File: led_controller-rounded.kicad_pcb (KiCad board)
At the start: 2 copper layers, 88.9 x 46.2 mm, 83 parts, among them J1 Screw_Terminal_01x02, J10 Conn_01x03, J2 SJ-3524-SMT, J3 Conn_01x03, J4 Conn_01x03, J5 Conn_01x03, J6 Conn_01x03, J7 Conn_01x03, J8 Conn_01x03, J9 Conn_01x03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

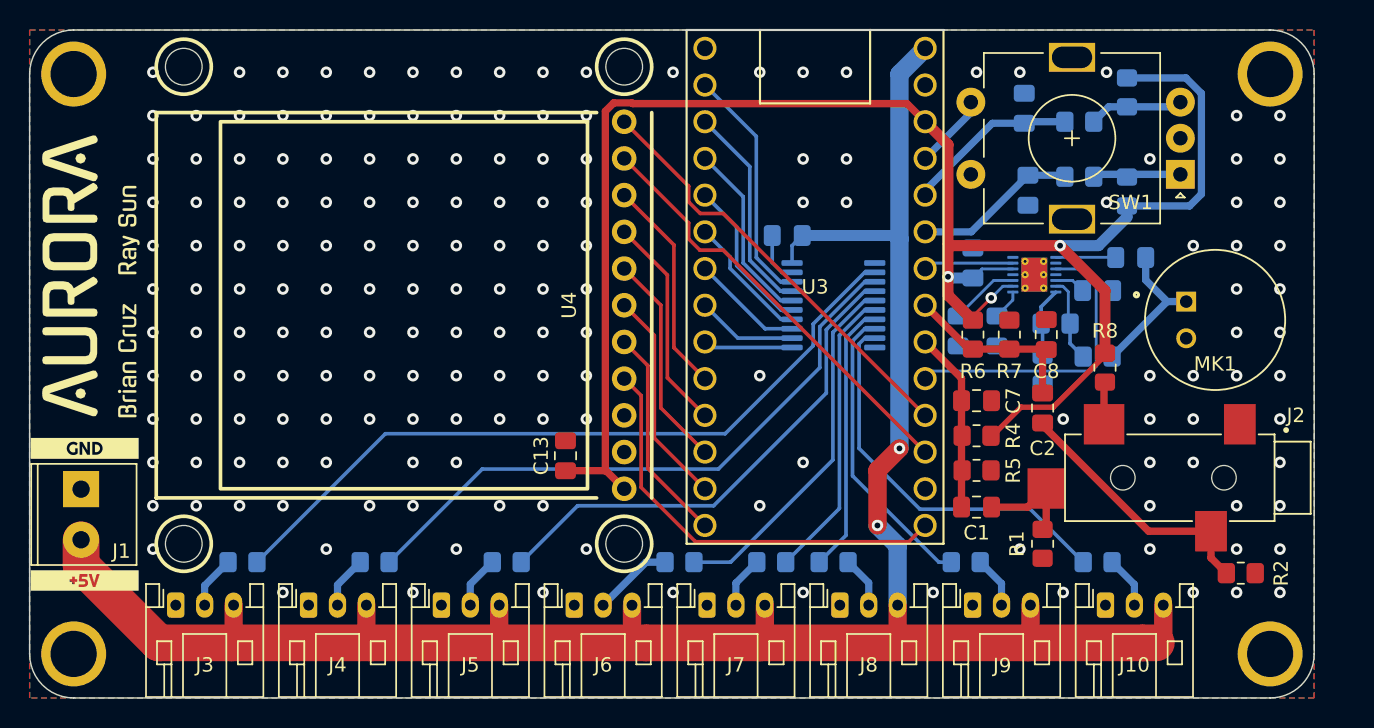
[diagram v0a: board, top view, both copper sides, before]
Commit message: Finish routing, add text, via grid, round tracks
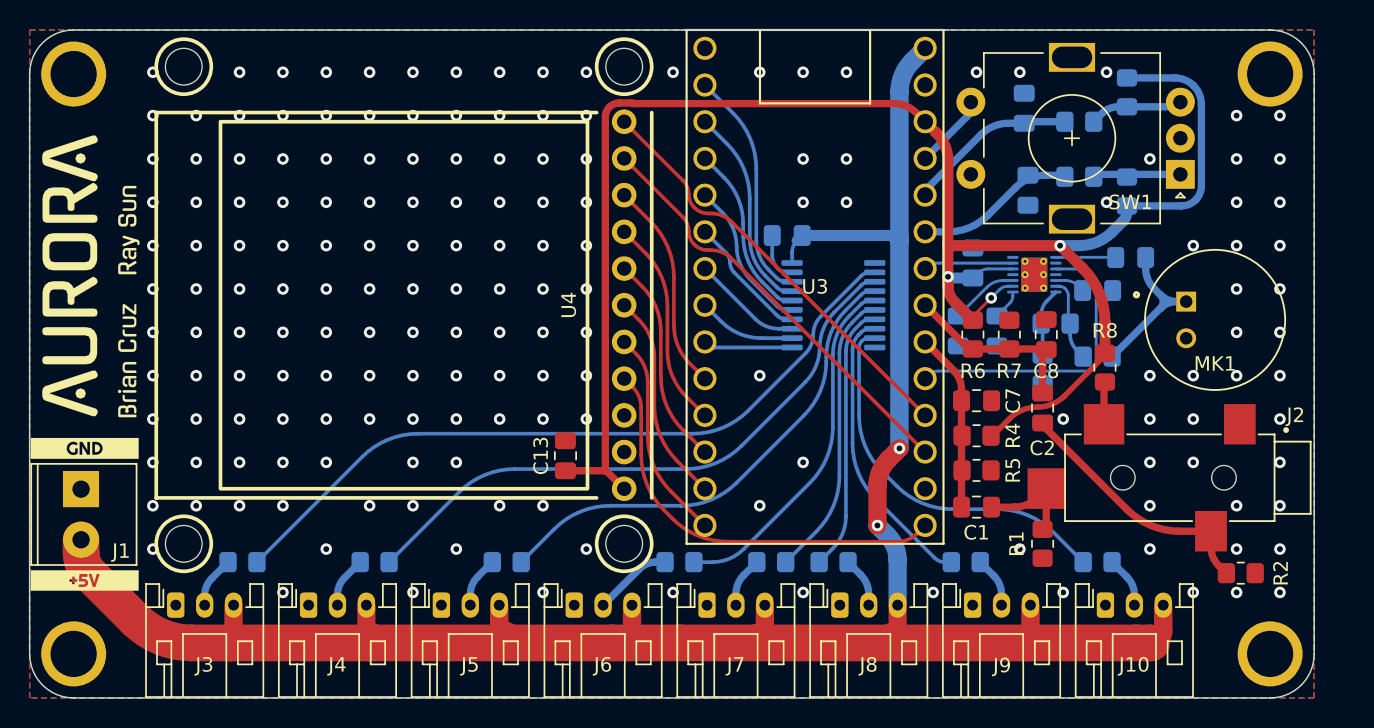
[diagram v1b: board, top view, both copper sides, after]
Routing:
- net +3V3: track 127.3 -> 125.6 mm
- net +5V: track 148.8 -> 150.4 mm
- net Net-(C3-Pad2): track 10.4 -> 11.8 mm
- net /AUD_L: track 7.24 -> 6.14 mm
- net Net-(R15-Pad2): track 34.8 -> 33.8 mm
- net Net-(R14-Pad2): track 43.3 -> 42.4 mm
- net Net-(R20-Pad2): track 27.3 -> 26.4 mm
- net /AUD_R: track 18.2 -> 17.4 mm
- net Net-(R13-Pad2): track 51.9 -> 51.2 mm
- net /SCK: track 29.7 -> 29.0 mm
- net Net-(R16-Pad2): track 25.2 -> 24.6 mm

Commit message: Rearrange some analog pins, tweak routing
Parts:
- C4: value 470n -> 0.47u
- moved R8 13.3 mm to (157.7, 121.9), turned to 180 degrees
- moved R2 12.3 mm to (168.4, 113.8)
- moved R1 7.62 mm to (160.5, 115.1), turned to 90 degrees
- moved C2 4.31 mm to (163.3, 110.2)
- moved C4 2.40 mm to (158.2, 110.1)
- moved C5 2.25 mm to (164.8, 107.3)
- moved C6 2.17 mm to (154.9, 110.1)
- moved C3 2.16 mm to (164.8, 104.4)
- moved R21 2.14 mm to (161.5, 109.6)
- moved R22 2.14 mm to (160.6, 112.7)
- moved R3 2.14 mm to (164.4, 111.8)
- moved U1 2.14 mm to (160.0, 106.2)
- moved C12 2.14 mm to (155.8, 105.4)
- moved C1 1.16 mm to (155.7, 119.0)
- moved C7 1.16 mm to (155.7, 111.6)
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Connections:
- C1 pad 1: /AUD_L_ADC -> /AUD_R_ADC
- C1 pad 2: /AUD_L -> /AUD_R
- C2 pad 1: /AUD_R_ADC -> /AUD_L_ADC
- C2 pad 2: /AUD_R -> /AUD_L
- C7 pad 1: /AUD_L_ADC -> /AUD_R_ADC
- C8 pad 1: /AUD_R_ADC -> /AUD_L_ADC
- J2 pad 2: Net-(J2-Pad2) -> /AUD_L
- J2 pad 4: /AUD_L -> /AUD_DET
- R1 pad 1: /AUD_L -> /AUD_R
- R2 pad 1: /AUD_R -> /AUD_L
- R4 pad 2: /AUD_L_ADC -> /AUD_R_ADC
- R5 pad 1: /AUD_L_ADC -> /AUD_R_ADC
- R6 pad 2: /AUD_R_ADC -> /AUD_L_ADC
- R7 pad 1: /AUD_R_ADC -> /AUD_L_ADC
- R8 pad 2: Net-(J2-Pad2) -> /AUD_DET
- U3 pad 21: unconnected-(U3-Pad21) -> /AUD_DET
- U3 pad 24: /MIC_GAIN -> /AUD_R_ADC
- U3 pad 26: /AUD_R_ADC -> /MIC_ADC
- U3 pad 27: /MIC_ADC -> /MIC_GAIN
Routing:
- net /AUD_DET: track 0.00 -> 10.9 mm
- net /MIC_GAIN: track 21.0 -> 17.7 mm
- net Net-(J2-Pad2): track 2.94 -> 0.00 mm
- net /AUD_R_ADC: track 12.7 -> 9.98 mm
- net Net-(C3-Pad1): track 4.15 -> 2.49 mm
- net /AUD_L_ADC: track 12.4 -> 11.4 mm
- net +3V3: track 125.6 -> 126.5 mm, vias 3 -> 5
- net /AUD_R: track 17.4 -> 18.3 mm
- net /AUD_L: track 6.14 -> 6.87 mm
- net /LED_OUT_2: track 3.52 -> 4.13 mm
- net /LED_OUT_7: track 3.53 -> 4.13 mm
- net /LED_OUT_1: track 3.54 -> 4.14 mm
- net /LED_OUT_0: track 3.57 -> 4.15 mm
- net /LED_OUT_6: track 3.50 -> 4.07 mm
- net Net-(U2-Pad14): track 8.86 -> 9.43 mm
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
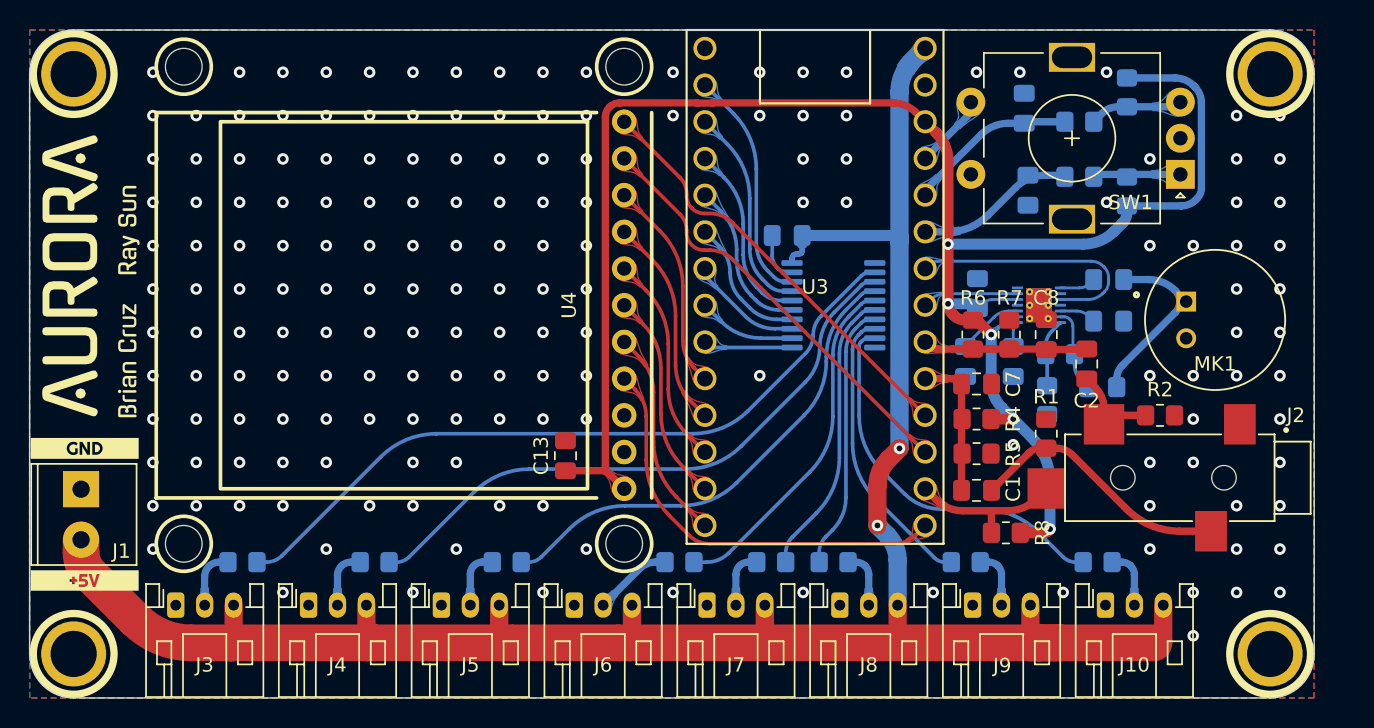
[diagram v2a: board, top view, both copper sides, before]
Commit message: Fix some clearance issues
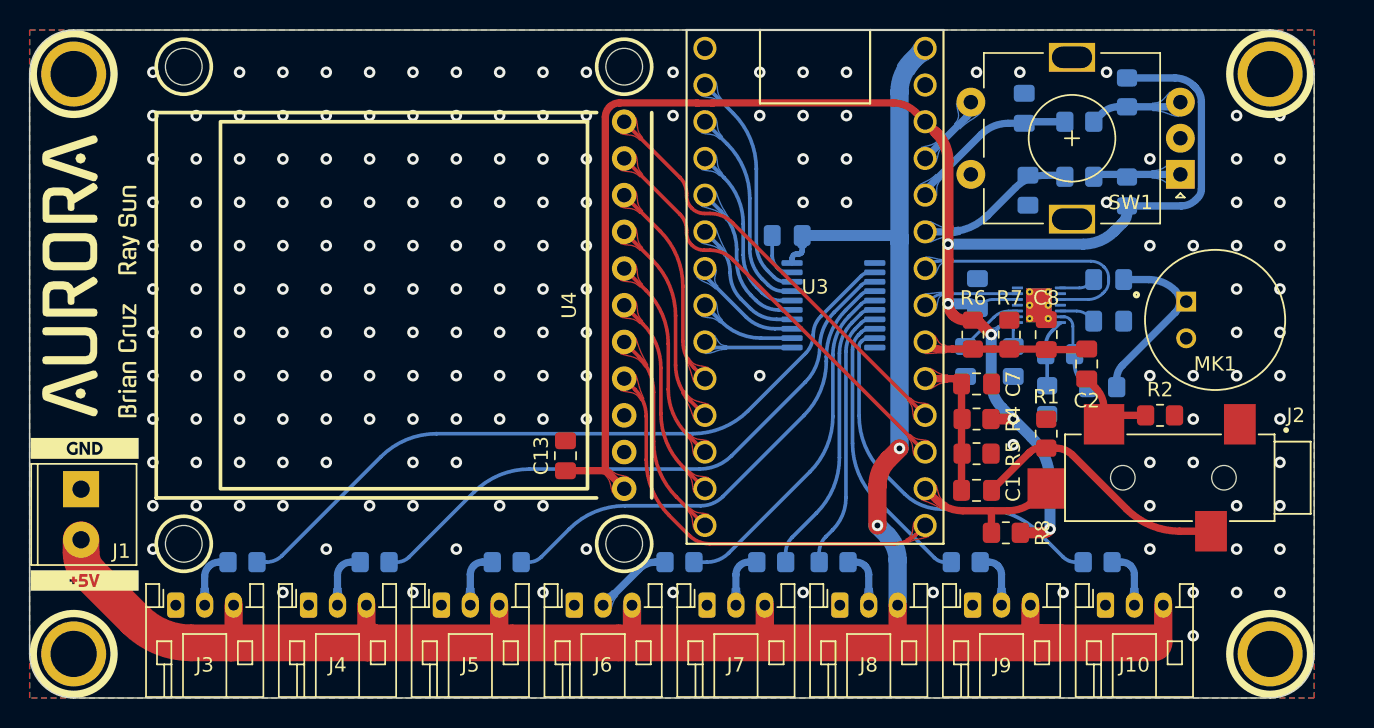
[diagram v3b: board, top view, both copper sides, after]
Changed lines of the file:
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@@
   (segment (start 156.718 108.204) (end 156.718 111.444369) (width 0.762) (layer "B.Cu") (net 13))
   (segment (start 157.744055 107.177944) (end 156.718 108.204) (width 0.2) (layer "B.Cu") (net 13))
-  (segment (start 170.856755 98.891244) (end 170.985198 98.762801) (width 0.508) (layer "B.Cu") (net 13))
+  (segment (start 170.856755 98.891244) (end 171.018581 98.729418) (width 0.508) (layer "B.Cu") (net 13))
   (segment (start 160.784857 121.663143) (end 160.787714 121.660286) (width 0.762) (layer "B.Cu") (net 13))
   (segment (start 165.807693 100.478328) (end 165.228261 101.057761) (width 0.762) (layer "B.Cu") (net 13))
@@
   (segment (start 158.24125 106.972) (end 158.5325 106.972) (width 0.2) (layer "B.Cu") (net 13))
   (segment (start 169.431896 90.44) (end 166.116 90.44) (width 0.508) (layer "B.Cu") (net 13))
-  (segment (start 171.263511 92.144906) (end 171.263511 98.090895) (width 0.508) (layer "B.Cu") (net 13))
+  (segment (start 171.263511 92.102434) (end 171.263511 98.138105) (width 0.508) (layer "B.Cu") (net 13))
   (segment (start 156.84133 105.772) (end 158.5325 105.772) (width 0.2) (layer "B.Cu") (net 13))
   (segment (start 170.727043 90.976467) (end 170.816639 91.066063) (width 0.508) (layer "B.Cu") (net 13))
+  (segment (start 170.816639 91.066063) (end 170.846672 91.096096) (width 0.508) (layer "B.Cu") (net 13))
   (arc (start 170.727043 90.976467) (mid 170.132824 90.579423) (end 169.431896 90.44) (width 0.508) (layer "B.Cu") (net 13))
   (arc (start 170.856755 98.891244) (mid 170.406212 99.192287) (end 169.87476 99.298) (width 0.508) (layer "B.Cu") (net 13))
@@
   (arc (start 159.512 115.316) (mid 160.451937 116.722716) (end 160.782 118.382051) (width 0.762) (layer "B.Cu") (net 13))
   (arc (start 166.116 99.734011) (mid 166.035873 100.136832) (end 165.807693 100.478328) (width 0.762) (layer "B.Cu") (net 13))
-  (arc (start 171.263511 98.090895) (mid 171.19118 98.454528) (end 170.985198 98.762801) (width 0.508) (layer "B.Cu") (net 13))
+  (arc (start 171.263511 98.138105) (mid 171.199856 98.458121) (end 171.018581 98.729418) (width 0.508) (layer "B.Cu") (net 13))
   (arc (start 156.84133 105.772) (mid 156.429436 105.85393) (end 156.08025 106.08725) (width 0.2) (layer "B.Cu") (net 13))
   (arc (start 160.782 121.661959) (mid 160.783033 121.663505) (end 160.784857 121.663143) (width 0.762) (layer "B.Cu") (net 13))
@@
   (arc (start 155.5995 106.237) (mid 155.764999 106.305552) (end 155.930499 106.237) (width 0.762) (layer "B.Cu") (net 13))
   (arc (start 155.5995 106.237) (mid 155.416184 106.114512) (end 155.199949 106.071501) (width 0.762) (layer "B.Cu") (net 13))
-  (arc (start 170.816639 91.066063) (mid 171.147372 91.56104) (end 171.263511 92.144906) (width 0.508) (layer "B.Cu") (net 13))
+  (arc (start 170.846672 91.096096) (mid 171.155177 91.557808) (end 171.263511 92.102434) (width 0.508) (layer "B.Cu") (net 13))
   (arc (start 165.228261 101.057761) (mid 164.244956 101.714784) (end 163.085069 101.9455) (width 0.762) (layer "B.Cu") (net 13))
   (segment (start 131.70041 129.54) (end 130.935589 129.54) (width 2.54) (layer "F.Cu") (net 14))
@@
   (arc (start 104.037524 129.54) (mid 104.132199 129.521167) (end 104.212461 129.467539) (width 2.54) (layer "F.Cu") (net 14))
   (arc (start 131.85881 128.616779) (mid 131.788534 128.97008) (end 131.588405 129.269595) (width 1.27) (layer "F.Cu") (net 14))
-  (arc (start 160.02 129.54) (mid 160.02 129.54) (end 160.02 129.54) (width 2.54) (layer "F.Cu") (net 14))
   (segment (start 151.257 89.281) (end 152.146 88.392) (width 1.27) (layer "B.Cu") (net 14))
   (segment (start 150.368 116.078) (end 150.368 101.779605) (width 1.27) (layer "B.Cu") (net 14))
@@
   (arc (start 118.331963 115.062) (mid 116.249572 115.476213) (end 114.484207 116.655792) (width 0.254) (layer "B.Cu") (net 27))
   (arc (start 148.313155 103.897) (mid 147.994097 103.960464) (end 147.723614 104.141195) (width 0.254) (layer "B.Cu") (net 27))
-  (segment (start 135.580405 117.508511) (end 124.775452 117.508511) (width 0.254) (layer "B.Cu") (net 28))
+  (segment (start 136.536732 117.508511) (end 124.775452 117.508511) (width 0.254) (layer "B.Cu") (net 28))
   (segment (start 145.852753 106.662056) (end 147.723614 104.791195) (width 0.254) (layer "B.Cu") (net 28))
   (segment (start 148.313155 104.547) (end 148.6585 104.547) (width 0.254) (layer "B.Cu") (net 28))
   (segment (start 115.562 123.952) (end 115.046 123.952) (width 0.254) (layer "B.Cu") (net 28))
-  (segment (start 143.853006 111.489873) (end 139.428161 115.914718) (width 0.254) (layer "B.Cu") (net 28))
+  (segment (start 143.853006 111.489873) (end 138.751935 116.590944) (width 0.254) (layer "B.Cu") (net 28))
   (segment (start 116.442867 123.587132) (end 120.927696 119.102303) (width 0.254) (layer "B.Cu") (net 28))
   (arc (start 144.85288 109.075965) (mid 144.593021 110.382362) (end 143.853006 111.489873) (width 0.254) (layer "B.Cu") (net 28))
   (arc (start 124.775452 117.508511) (mid 122.693061 117.922724) (end 120.927696 119.102303) (width 0.254) (layer "B.Cu") (net 28))
-  (arc (start 139.428161 115.914718) (mid 137.662795 117.094297) (end 135.580405 117.508511) (width 0.254) (layer "B.Cu") (net 28))
+  (arc (start 138.751935 116.590944) (mid 137.735591 117.270043) (end 136.536732 117.508511) (width 0.254) (layer "B.Cu") (net 28))
   (arc (start 145.852753 106.662056) (mid 145.112738 107.769566) (end 144.85288 109.075965) (width 0.254) (layer "B.Cu") (net 28))
   (arc (start 148.313155 104.547) (mid 147.994097 104.610464) (end 147.723614 104.791195) (width 0.254) (layer "B.Cu") (net 28))
@@
   (segment (start 124.706 123.952) (end 124.19 123.952) (width 0.254) (layer "B.Cu") (net 29))
   (segment (start 145.3064 110.054005) (end 145.3064 109.740311) (width 0.254) (layer "B.Cu") (net 29))
-  (segment (start 135.253525 120.048511) (end 131.379452 120.048511) (width 0.254) (layer "B.Cu") (net 29))
+  (segment (start 136.610991 120.048511) (end 131.379452 120.048511) (width 0.254) (layer "B.Cu") (net 29))
   (segment (start 147.723614 105.441195) (end 146.637105 106.527705) (width 0.254) (layer "B.Cu") (net 29))
-  (segment (start 143.753879 113.802119) (end 139.101281 118.454718) (width 0.254) (layer "B.Cu") (net 29))
+  (segment (start 143.753879 113.802119) (end 138.141407 119.414592) (width 0.254) (layer "B.Cu") (net 29))
   (segment (start 127.531695 121.642303) (end 125.586867 123.587132) (width 0.254) (layer "B.Cu") (net 29))
   (arc (start 125.586867 123.587132) (mid 125.182721 123.857173) (end 124.706 123.952) (width 0.254) (layer "B.Cu") (net 29))
@@
   (arc (start 148.313155 105.197) (mid 147.994097 105.260464) (end 147.723614 105.441195) (width 0.254) (layer "B.Cu") (net 29))
   (arc (start 145.3064 110.054005) (mid 144.902912 112.082469) (end 143.753879 113.802119) (width 0.254) (layer "B.Cu") (net 29))
-  (arc (start 139.101281 118.454718) (mid 137.335915 119.634297) (end 135.253525 120.048511) (width 0.254) (layer "B.Cu") (net 29))
+  (arc (start 138.141407 119.414592) (mid 137.439246 119.883761) (end 136.610991 120.048511) (width 0.254) (layer "B.Cu") (net 29))
   (arc (start 131.379452 120.048511) (mid 129.297061 120.462724) (end 127.531695 121.642303) (width 0.254) (layer "B.Cu") (net 29))
   (segment (start 148.313155 105.847) (end 148.6585 105.847) (width 0.254) (layer "B.Cu") (net 30))

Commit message: some more tweaks
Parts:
- moved J2 2.29 mm to (175.1, 118.1)
- moved R2 2.29 mm to (170.7, 113.8)
- moved C1 0.87 mm to (156.6, 119.0)
- moved C7 0.87 mm to (156.6, 111.6)
- moved R1 0.87 mm to (161.4, 115.1)
- moved R4 0.87 mm to (156.6, 114.0)
- moved R5 0.87 mm to (156.6, 116.4)
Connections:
- U3 pad 22: /CS_SD -> /AUD_R_ADC
- U3 pad 23: /BACKLIGHT -> /AUD_L_ADC
- U3 pad 24: /AUD_R_ADC -> /CS_SD
- U3 pad 25: /AUD_L_ADC -> /BACKLIGHT
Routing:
- net GND: track 3.43 -> 0.00 mm, vias 176 -> 175
- net /CS_SD: track 29.7 -> 26.5 mm
- net /BACKLIGHT: track 29.7 -> 26.5 mm
- net /AUD_L_ADC: track 11.4 -> 14.3 mm
- net /AUD_DET: track 10.9 -> 13.2 mm
- net +5V: track 150.5 -> 152.6 mm
- net /AUD_R: track 18.3 -> 19.7 mm
- net /AUD_L: track 6.87 -> 7.83 mm
- net /AUD_R_ADC: track 9.98 -> 10.8 mm
- net +3V3: track 126.5 -> 125.9 mm
- net Net-(R13-Pad2): track 51.1 -> 50.6 mm
